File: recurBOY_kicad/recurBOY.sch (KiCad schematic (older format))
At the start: 26 parts, among them J1 CV_IN_0, J10 EURO_POWER, J2 CV_IN_1, J3 CV_IN_2, J4 CV_IN_3, J5 DISPLAY_1.8, J6 Conn_01x01, J7 VIDEO_OUT, J8 Raspberry_Pi_2_3, U1 MCP3208

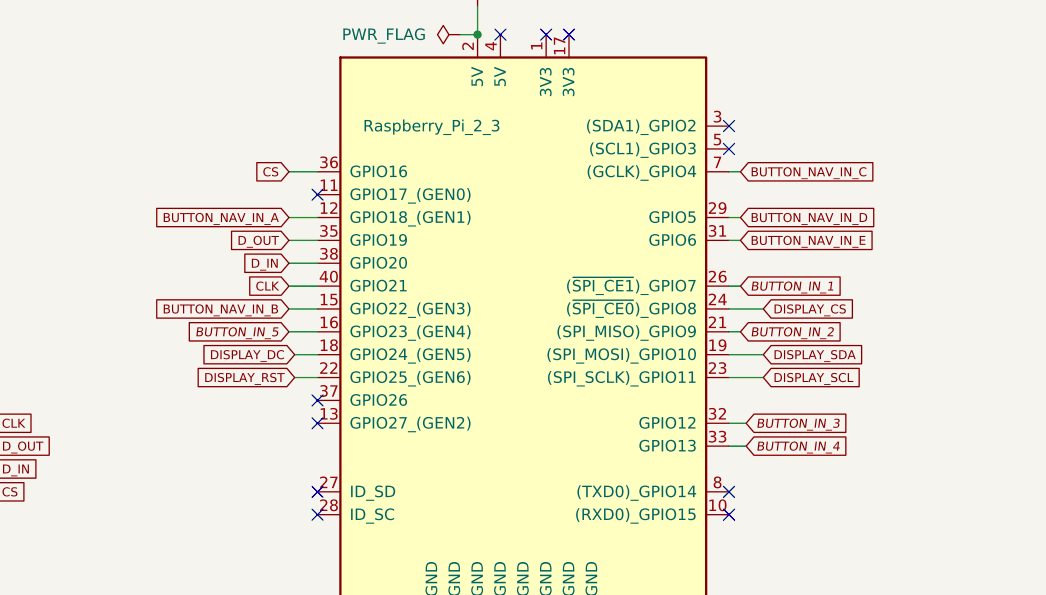
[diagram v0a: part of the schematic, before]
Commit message: updated kicad files and added booklet info
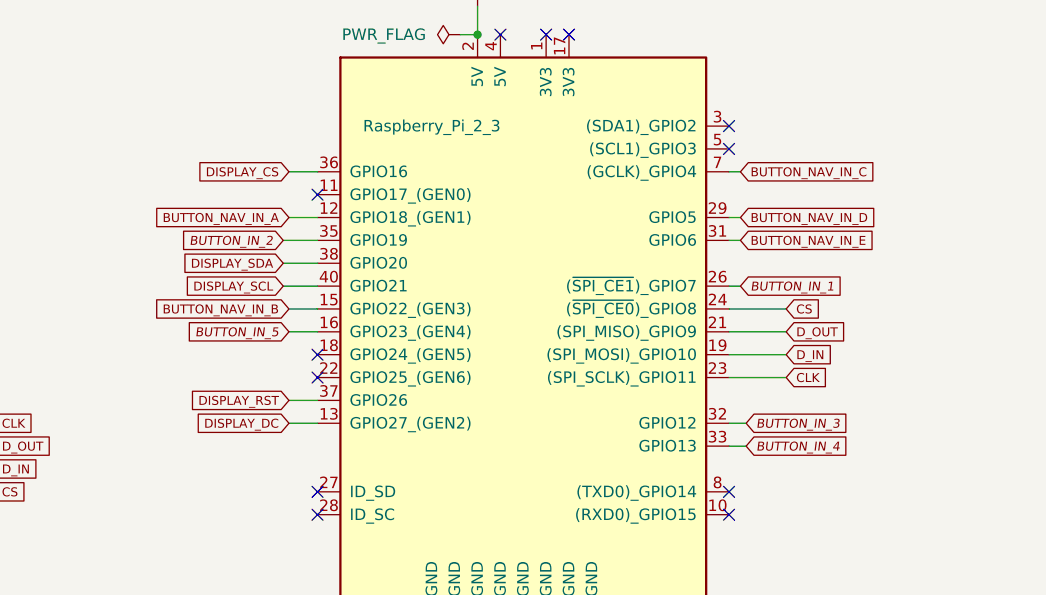
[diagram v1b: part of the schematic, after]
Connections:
- net BUTTON_IN_2: now also J8.35 (GPIO19); no longer J8.21 ((SPI_MISO)_GPIO9)
- net CLK: now also J8.23 ((SPI_SCLK)_GPIO11); no longer J8.40 (GPIO21)
- net CS: now also J8.24 ((~SPI_CE0~)_GPIO8); no longer J8.36 (GPIO16)
- net DISPLAY_CS: now also J8.36 (GPIO16); no longer J8.24 ((~SPI_CE0~)_GPIO8)
- net DISPLAY_DC: now also J8.13 (GPIO27_(GEN2)); no longer J8.18 (GPIO24_(GEN5))
- net DISPLAY_RST: now also J8.37 (GPIO26); no longer J8.22 (GPIO25_(GEN6))
- net DISPLAY_SCL: now also J8.40 (GPIO21); no longer J8.23 ((SPI_SCLK)_GPIO11)
- net DISPLAY_SDA: now also J8.38 (GPIO20); no longer J8.19 ((SPI_MOSI)_GPIO10)
- net D_IN: now also J8.19 ((SPI_MOSI)_GPIO10); no longer J8.38 (GPIO20)
- net D_OUT: now also J8.21 ((SPI_MISO)_GPIO9); no longer J8.35 (GPIO19)
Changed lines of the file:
@@
 	1    0    0    -1
 $EndComp
-Text GLabel 8675 4075 0    39   Input ~ 0
+Text GLabel 10850 4475 2    39   Input ~ 0
 CLK
-Text GLabel 8675 3875 0    39   Input ~ 0
+Text GLabel 10850 4275 2    39   Input ~ 0
 D_OUT
-Text GLabel 8675 3975 0    39   Input ~ 0
+Text GLabel 10850 4375 2    39   Input ~ 0
 D_IN
-Text GLabel 8675 3575 0    39   Input ~ 0
+Text GLabel 10850 4175 2    39   Input ~ 0
 CS
 $Comp
@@
 $EndComp
 NoConn ~ 8800 3675
-NoConn ~ 8800 4575
-NoConn ~ 8800 4675
 NoConn ~ 8800 4975
 NoConn ~ 8800 5075
@@
 	9300 5575 9300 5700
 Wire Wire Line
-	8675 3575 8800 3575
-Wire Wire Line
-	8675 3875 8800 3875
-Wire Wire Line
-	8675 3975 8800 3975
-Wire Wire Line
-	8675 4075 8800 4075
-Wire Wire Line
 	6325 7075 6325 7275
 Wire Wire Line
@@
 Wire Wire Line
 	10425 1350 10300 1350
-Text GLabel 10750 4475 2    39   Input ~ 0
+Text GLabel 8650 4075 0    39   Input ~ 0
 DISPLAY_SCL
-Text GLabel 10750 4375 2    39   Input ~ 0
+Text GLabel 8650 3975 0    39   Input ~ 0
 DISPLAY_SDA
-Text GLabel 8700 4475 0    39   Input ~ 0
+Text GLabel 8675 4575 0    39   Input ~ 0
 DISPLAY_RST
-Text GLabel 8700 4375 0    39   Input ~ 0
+Text GLabel 8675 4675 0    39   Input ~ 0
 DISPLAY_DC
-Text GLabel 10750 4175 2    39   Input ~ 0
+Text GLabel 8675 3575 0    39   Input ~ 0
 DISPLAY_CS
 NoConn ~ 10425 1150
@@
 	10300 1250 10425 1250
 Wire Wire Line
-	8700 4375 8800 4375
-Wire Wire Line
-	8700 4475 8800 4475
-Wire Wire Line
-	10750 4175 10600 4175
-Wire Wire Line
-	10750 4375 10600 4375
-Wire Wire Line
-	10750 4475 10600 4475
+	10600 4175 10850 4175
+Wire Wire Line
+	10600 4375 10850 4375
+Wire Wire Line
+	10600 4475 10850 4475
 NoConn ~ 10600 5075
 Text GLabel 8675 3775 0    39   Input ~ 0
@@
 Text GLabel 10650 4075 2    39   Input Italic 0
 BUTTON_IN_1
-Text GLabel 10650 4275 2    39   Input Italic 0
+Text GLabel 8650 3875 0    39   Input Italic 0
 BUTTON_IN_2
 Text GLabel 10675 4675 2    39   Input Italic 0
@@
 	10650 4075 10600 4075
 Wire Wire Line
-	10650 4275 10600 4275
+	10600 4275 10850 4275
 NoConn ~ 9800 2975
 Wire Wire Line
@@
 Wire Wire Line
 	8800 4275 8675 4275
+Wire Wire Line
+	8675 4575 8800 4575
+Wire Wire Line
+	8675 4675 8800 4675
+Wire Wire Line
+	8650 4075 8800 4075
+Wire Wire Line
+	8650 3975 8800 3975
+Wire Wire Line
+	8650 3875 8800 3875
+Wire Wire Line
+	8675 3575 8800 3575
+NoConn ~ 8800 4375
+NoConn ~ 8800 4475
 $EndSCHEMATC
